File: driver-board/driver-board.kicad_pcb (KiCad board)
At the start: 2 copper layers, 85 x 58 mm, 57 parts, among them J1 MCP4725, J2 Conn_Coaxial, J3 MCP4725, J4 Conn_Coaxial, SW1 RST, SW2 BIAS ON/OF, U1 Pico, U2 MIC5317, U3 TSV358, U4 TSV358, U5 TCBT-2R5G, U6 LM2904, U7 LT3462A

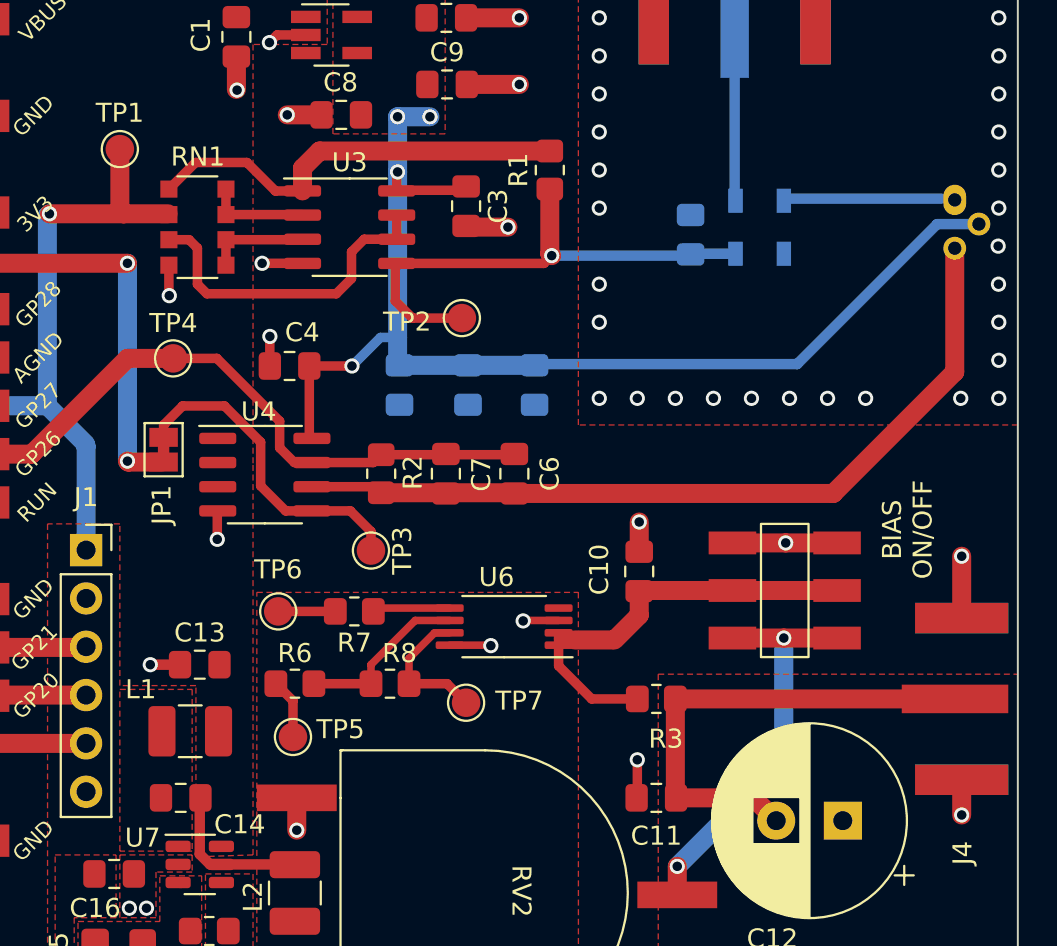
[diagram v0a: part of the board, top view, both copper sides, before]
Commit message: fixed RN1 fp
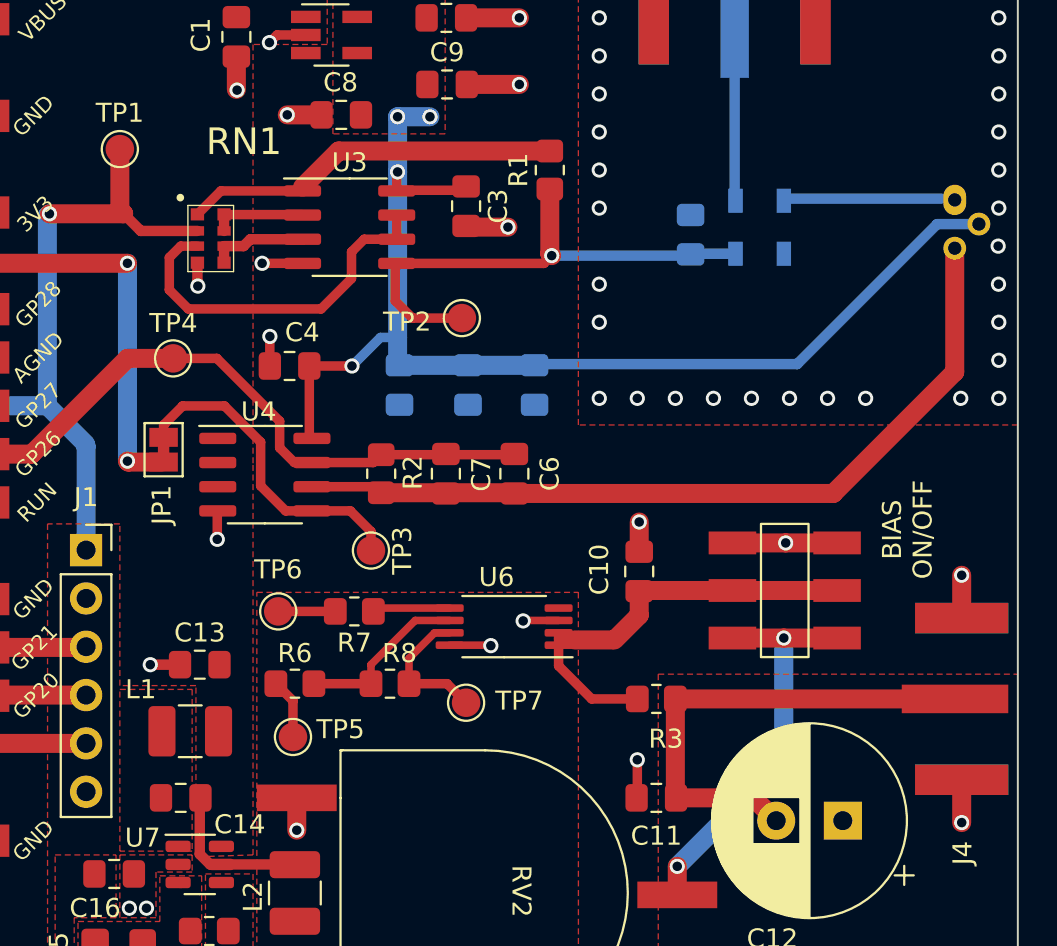
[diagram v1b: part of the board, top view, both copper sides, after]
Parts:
- RN1: footprint Resistor_SMD:R_Array_Convex_4x1206 -> lib:ACASA5002S5002P1AT
- moved RN1 0.60 mm to (99.9, 85.4)
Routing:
- net Net-(R1-Pad2): track 22.8 -> 19.8 mm
- net DAC_OUT_I_SRC: track 32.8 -> 34.7 mm
- net Net-(RN1-Pad3): track 17.5 -> 19.4 mm
- net GND: track 49.3 -> 48.3 mm

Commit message: fixed U2-EN pin
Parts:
- removed TP2: TestPoint, TestPoint:TestPoint_Pad_D1.5mm
- added JP2: SolderJumper_2_Bridged, Jumper:SolderJumper-2_P1.3mm_Bridged_Pad1.0x1.5mm, F.Cu at (118.4, 88.6)
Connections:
- R1 pad 1: Net-(C5-Pad2) -> Net-(R1-Pad1)
- U2 pad 3: unconnected-(U2-Pad3) -> 5V
- U3 pad 5: Net-(C5-Pad2) -> Net-(R1-Pad1)
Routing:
- net Net-(C5-Pad2): track 27.3 -> 14.2 mm
- net Net-(R1-Pad1): track 0.00 -> 12.0 mm
- net 5V: track 0.00 -> 4.50 mm
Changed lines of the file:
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@@
   (net 9 "unconnected-(U1-Pad34)")
   (net 10 "unconnected-(U2-Pad4)")
-  (net 11 "unconnected-(U2-Pad3)")
+  (net 11 "Net-(R1-Pad1)")
   (net 12 "Net-(RN1-Pad7)")
   (net 13 "A3V3")
@@
     (fp_line (start -1 -0.625) (end 1 -0.625) (layer "F.Fab") (width 0.1))
     (pad "1" smd roundrect locked (at -1 0 90) (size 1.2 1.4) (layers "F.Cu" "F.Paste" "F.Mask") (roundrect_rratio 0.2083333333)
-      (net 14 "Net-(C5-Pad2)") (pintype "passive"))
+      (net 11 "Net-(R1-Pad1)") (pintype "passive"))
     (pad "2" smd roundrect locked (at 1 0 90) (size 1.2 1.4) (layers "F.Cu" "F.Paste" "F.Mask") (roundrect_rratio 0.2083333333)
       (net 6 "Net-(R1-Pad2)") (pintype "passive"))
@@
       (net 2 "GND") (pinfunction "GND") (pintype "passive"))
     (pad "3" smd rect locked (at -1.35 0.95) (size 1.56 0.65) (layers "F.Cu" "F.Paste" "F.Mask")
-      (net 11 "unconnected-(U2-Pad3)") (pinfunction "EN") (pintype "passive+no_connect"))
+      (net 1 "5V") (pinfunction "EN") (pintype "passive"))
     (pad "4" smd rect locked (at 1.35 0.95) (size 1.56 0.65) (layers "F.Cu" "F.Paste" "F.Mask")
       (net 10 "unconnected-(U2-Pad4)") (pinfunction "NC") (pintype "no_connect"))
@@
   )
   (footprint "Jumper:SolderJumper-2_P1.3mm_Bridged_Pad1.0x1.5mm" (layer "F.Cu")
+    (at 118.4 88.6 -90)
+    (descr "SMD Solder Jumper, 1x1.5mm Pads, 0.3mm gap, bridged with 1 copper strip")
+    (tags "net tie solder jumper bridged")
+    (property "Sheetfile" "driver-board.kicad_sch")
+    (property "Sheetname" "")
+    (attr exclude_from_pos_files)
+    (fp_text reference "JP2" (at 0 -1.8 90) (layer "F.SilkS")
+      (effects (font (size 1 1) (thickness 0.15)))
+    )
+    (fp_text value "SolderJumper_2_Bridged" (at 0 1.9 90) (layer "F.Fab")
+      (effects (font (size 1 1) (thickness 0.15)))
+    )
+    (fp_poly (pts
+        (xy -0.25 -0.3)
+        (xy 0.25 -0.3)
+        (xy 0.25 0.3)
+        (xy -0.25 0.3)
+      ) (layer "F.Cu") (width 0) (fill solid))
+    (fp_line (start -1.4 -1) (end 1.4 -1) (layer "F.SilkS") (width 0.12))
+    (fp_line (start -1.4 1) (end -1.4 -1) (layer "F.SilkS") (width 0.12))
+    (fp_line (start 1.4 -1) (end 1.4 1) (layer "F.SilkS") (width 0.12))
+    (fp_line (start 1.4 1) (end -1.4 1) (layer "F.SilkS") (width 0.12))
+    (fp_line (start 1.65 1.25) (end -1.65 1.25) (layer "F.CrtYd") (width 0.05))
+    (fp_line (start -1.65 -1.25) (end -1.65 1.25) (layer "F.CrtYd") (width 0.05))
+    (fp_line (start 1.65 1.25) (end 1.65 -1.25) (layer "F.CrtYd") (width 0.05))
+    (fp_line (start -1.65 -1.25) (end 1.65 -1.25) (layer "F.CrtYd") (width 0.05))
+    (pad "1" smd rect locked (at -0.65 0 270) (size 1 1.5) (layers "F.Cu" "F.Mask")
+      (net 11 "Net-(R1-Pad1)") (pinfunction "A") (pintype "passive"))
+    (pad "2" smd rect locked (at 0.65 0 270) (size 1 1.5) (layers "F.Cu" "F.Mask")
+      (net 14 "Net-(C5-Pad2)") (pinfunction "B") (pintype "passive"))
+  )
+  (footprint "Jumper:SolderJumper-2_P1.3mm_Bridged_Pad1.0x1.5mm" (layer "F.Cu")
     (at 98.1 97.7 90)
     (descr "SMD Solder Jumper, 1x1.5mm Pads, 0.3mm gap, bridged with 1 copper strip")
@@
       (net 2 "GND") (pinfunction "V-") (pintype "power_in"))
     (pad "5" smd roundrect (at 2.475 1.905) (size 1.95 0.6) (layers "F.Cu" "F.Paste" "F.Mask") (roundrect_rratio 0.25)
-      (net 14 "Net-(C5-Pad2)") (pinfunction "+") (pintype "input"))
+      (net 11 "Net-(R1-Pad1)") (pinfunction "+") (pintype "input"))
     (pad "6" smd roundrect (at 2.475 0.635) (size 1.95 0.6) (layers "F.Cu" "F.Paste" "F.Mask") (roundrect_rratio 0.25)
       (net 7 "Net-(RN1-Pad3)") (pinfunction "-") (pintype "input"))
@@
     (fp_circle (center 0 0) (end 3.45 0) (layer "F.CrtYd") (width 0.05) (fill none))
     (pad "" np_thru_hole circle locked (at 0 0) (size 3.2 3.2) (drill 3.2) (layers *.Cu *.Mask))
-  )
-  (footprint "TestPoint:TestPoint_Pad_D1.5mm" (layer "F.Cu")
-    (at 113.7775 90.7825)
-    (descr "SMD pad as test Point, diameter 1.5mm")
-    (tags "test point SMD pad")
-    (property "Sheetfile" "driver-board.kicad_sch")
-    (property "Sheetname" "")
-    (attr exclude_from_pos_files)
-    (fp_text reference "TP2" (at -2.8775 0.1975) (layer "F.SilkS")
-      (effects (font (size 1 1) (thickness 0.15)))
-    )
-    (fp_text value "TestPoint" (at 0 1.75) (layer "F.Fab")
-      (effects (font (size 1 1) (thickness 0.15)))
-    )
-    (fp_text user "${REFERENCE}" (at 0 -1.65) (layer "F.Fab")
-      (effects (font (size 1 1) (thickness 0.15)))
-    )
-    (fp_circle (center 0 0) (end 0 0.95) (layer "F.SilkS") (width 0.12) (fill none))
-    (fp_circle (center 0 0) (end 1.25 0) (layer "F.CrtYd") (width 0.05) (fill none))
-    (pad "1" smd circle locked (at 0 0) (size 1.5 1.5) (layers "F.Cu" "F.Mask")
-      (net 14 "Net-(C5-Pad2)") (pinfunction "1") (pintype "passive"))
   )
   (footprint "Package_TO_SOT_SMD:TSOT-23-6" (layer "F.Cu")
@@
     (effects (font (size 1 1) (thickness 0.15)))
   )
+  (segment (start 106.9 76.805) (end 106.855 76.85) (width 0.5) (layer "F.Cu") (net 1))
+  (segment (start 106.9 74.995) (end 106.9 76.805) (width 0.5) (layer "F.Cu") (net 1))
+  (segment (start 106.855 76.85) (end 105.575 76.85) (width 0.5) (layer "F.Cu") (net 1))
+  (segment (start 106.855 74.95) (end 106.9 74.995) (width 0.5) (layer "F.Cu") (net 1))
+  (segment (start 105.575 74.95) (end 106.855 74.95) (width 0.5) (layer "F.Cu") (net 1))
   (segment (start 123 114) (end 123 115.9625) (width 0.5) (layer "F.Cu") (net 2))
   (segment (start 103.6625 76.3) (end 104.0625 75.9) (width 0.5) (layer "F.Cu") (net 2))
@@
   (via (at 116.8 78.5) (size 0.8) (drill 0.5) (layers "F.Cu" "B.Cu") (net 2))
   (via (at 140.05 117.3) (size 0.8) (drill 0.5) (layers "F.Cu" "B.Cu") (net 2))
-  (via (at 121 91) (size 0.8) (drill 0.5) (layers "F.Cu" "B.Cu") (free) (net 2))
+  (via (at 121 89) (size 0.8) (drill 0.5) (layers "F.Cu" "B.Cu") (free) (net 2))
   (via (at 142 83) (size 0.8) (drill 0.5) (layers "F.Cu" "B.Cu") (free) (net 2))
   (via (at 125 95) (size 0.8) (drill 0.5) (layers "F.Cu" "B.Cu") (free) (net 2))
@@
   (via (at 121 75) (size 0.8) (drill 0.5) (layers "F.Cu" "B.Cu") (free) (net 2))
   (via (at 116.2 86) (size 0.8) (drill 0.5) (layers "F.Cu" "B.Cu") (free) (net 2))
-  (via (at 121 89) (size 0.8) (drill 0.5) (layers "F.Cu" "B.Cu") (free) (net 2))
+  (via (at 121 87) (size 0.8) (drill 0.5) (layers "F.Cu" "B.Cu") (free) (net 2))
   (via (at 121 81) (size 0.8) (drill 0.5) (layers "F.Cu" "B.Cu") (free) (net 2))
   (via (at 142 91) (size 0.8) (drill 0.5) (layers "F.Cu" "B.Cu") (free) (net 2))
@@
   (segment (start 101.2775 87.87) (end 101.2775 87) (width 0.55) (layer "F.Cu") (net 8))
   (segment (start 101.2775 87) (end 102.3 87) (width 0.55) (layer "F.Cu") (net 8))
+  (segment (start 118.4 84) (end 118.4 87.95) (width 1) (layer "F.Cu") (net 11))
+  (segment (start 110.3525 87.9075) (end 110.395 87.95) (width 0.5) (layer "F.Cu") (net 11))
+  (segment (start 110.395 87.95) (end 118.4 87.95) (width 0.5) (layer "F.Cu") (net 11))
   (segment (start 101.3775 85.3425) (end 105.3775 85.3425) (width 0.5) (layer "F.Cu") (net 12))
   (segment (start 101.2775 85.33) (end 101.2775 86.2) (width 0.55) (layer "F.Cu") (net 12))
@@
   (segment (start 108 93.3) (end 109.5 91.8) (width 0.5) (layer "B.Cu") (net 13))
   (segment (start 110.5 93.2625) (end 117.6 93.2625) (width 1) (layer "B.Cu") (net 13))
-  (segment (start 118.5 87.5) (end 118.4 87.4) (width 1) (layer "F.Cu") (net 14))
-  (segment (start 110.2775 87.9825) (end 110.3525 87.9075) (width 0.5) (layer "F.Cu") (net 14))
-  (segment (start 111.1775 90.7825) (end 110.2775 89.8825) (width 0.5) (layer "F.Cu") (net 14))
-  (segment (start 118.0925 87.9075) (end 110.3525 87.9075) (width 0.5) (layer "F.Cu") (net 14))
-  (segment (start 118.4 87.4) (end 118.4 84) (width 1) (layer "F.Cu") (net 14))
-  (segment (start 111.1775 90.7825) (end 113.7775 90.7825) (width 0.5) (layer "F.Cu") (net 14))
-  (segment (start 110.2775 89.8825) (end 110.2775 87.9825) (width 0.5) (layer "F.Cu") (net 14))
-  (segment (start 118.5 87.5) (end 118.0925 87.9075) (width 0.5) (layer "F.Cu") (net 14))
-  (via (at 118.5 87.5) (size 0.8) (drill 0.5) (layers "F.Cu" "B.Cu") (net 14))
-  (segment (start 118.5 87.5) (end 125.7375 87.5) (width 0.55) (layer "B.Cu") (net 14))
+  (segment (start 118.4 89.25) (end 118.4 91.1) (width 0.5) (layer "F.Cu") (net 14))
+  (via (at 118.4 91.1) (size 0.8) (drill 0.4) (layers "F.Cu" "B.Cu") (net 14))
+  (segment (start 118.4 91.1) (end 124 91.1) (width 0.5) (layer "B.Cu") (net 14))
+  (segment (start 125.8 89.3) (end 125.8 87.4375) (width 0.5) (layer "B.Cu") (net 14))
   (segment (start 125.8375 87.4) (end 128.16 87.4) (width 0.55) (layer "B.Cu") (net 14))
+  (segment (start 124 91.1) (end 125.8 89.3) (width 0.5) (layer "B.Cu") (net 14))
   (segment (start 133.3 100) (end 139.684724 93.615276) (width 1) (layer "F.Cu") (net 15))
   (segment (start 139.684724 93.615276) (end 139.684724 87.109448) (width 1) (layer "F.Cu") (net 15))

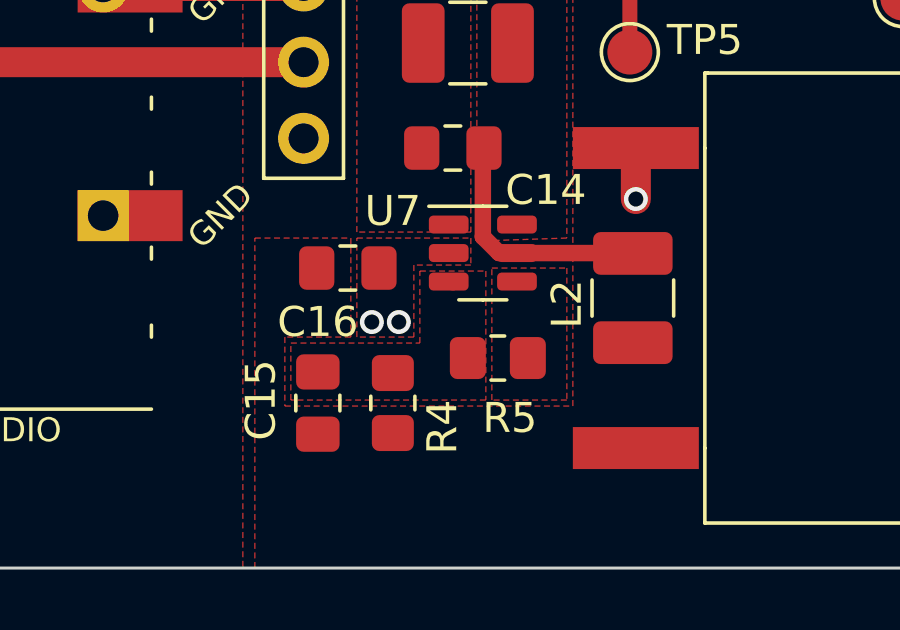
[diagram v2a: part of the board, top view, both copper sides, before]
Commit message: fixed lt3462 fp, routing pending
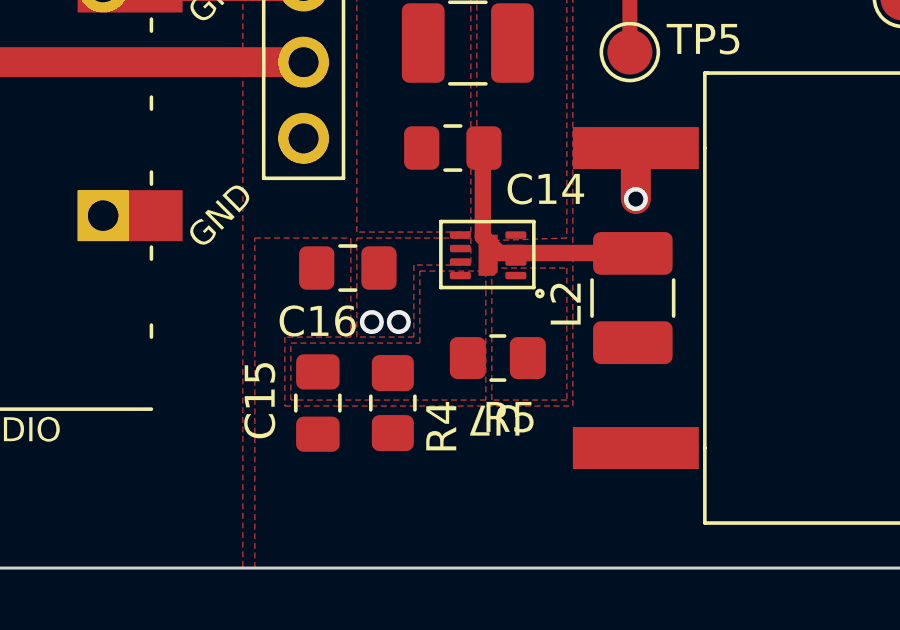
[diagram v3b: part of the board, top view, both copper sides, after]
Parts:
- U7: footprint Package_TO_SOT_SMD:TSOT-23-6 -> lib:LT3462A
- moved U7 1.33 mm to (101.1, 120.2), turned to 180 degrees
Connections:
- U7 pad 1: Net-(C14-Pad1) -> Net-(C15-Pad1)
- U7 pad 3: Net-(C15-Pad1) -> GND
- U7 pad 4: Net-(R5-Pad1) -> Net-(C14-Pad1)
- U7 pad 5: Net-(C14-Pad2) -> 5V
- U7 pad 6: 5V -> unconnected-(U7-Pad6)
